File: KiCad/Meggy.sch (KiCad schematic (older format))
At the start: 19 parts, among them J1 USB_B_Micro, J2 Conn_01x03, Q1 DMP2305U-7, Q2 DMP2305U-7, U1 ROM-socket-42pin, U2 AT90USB1286-MU, U3 M29F160F, X1 Standard_Clock_Oscillators_XT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

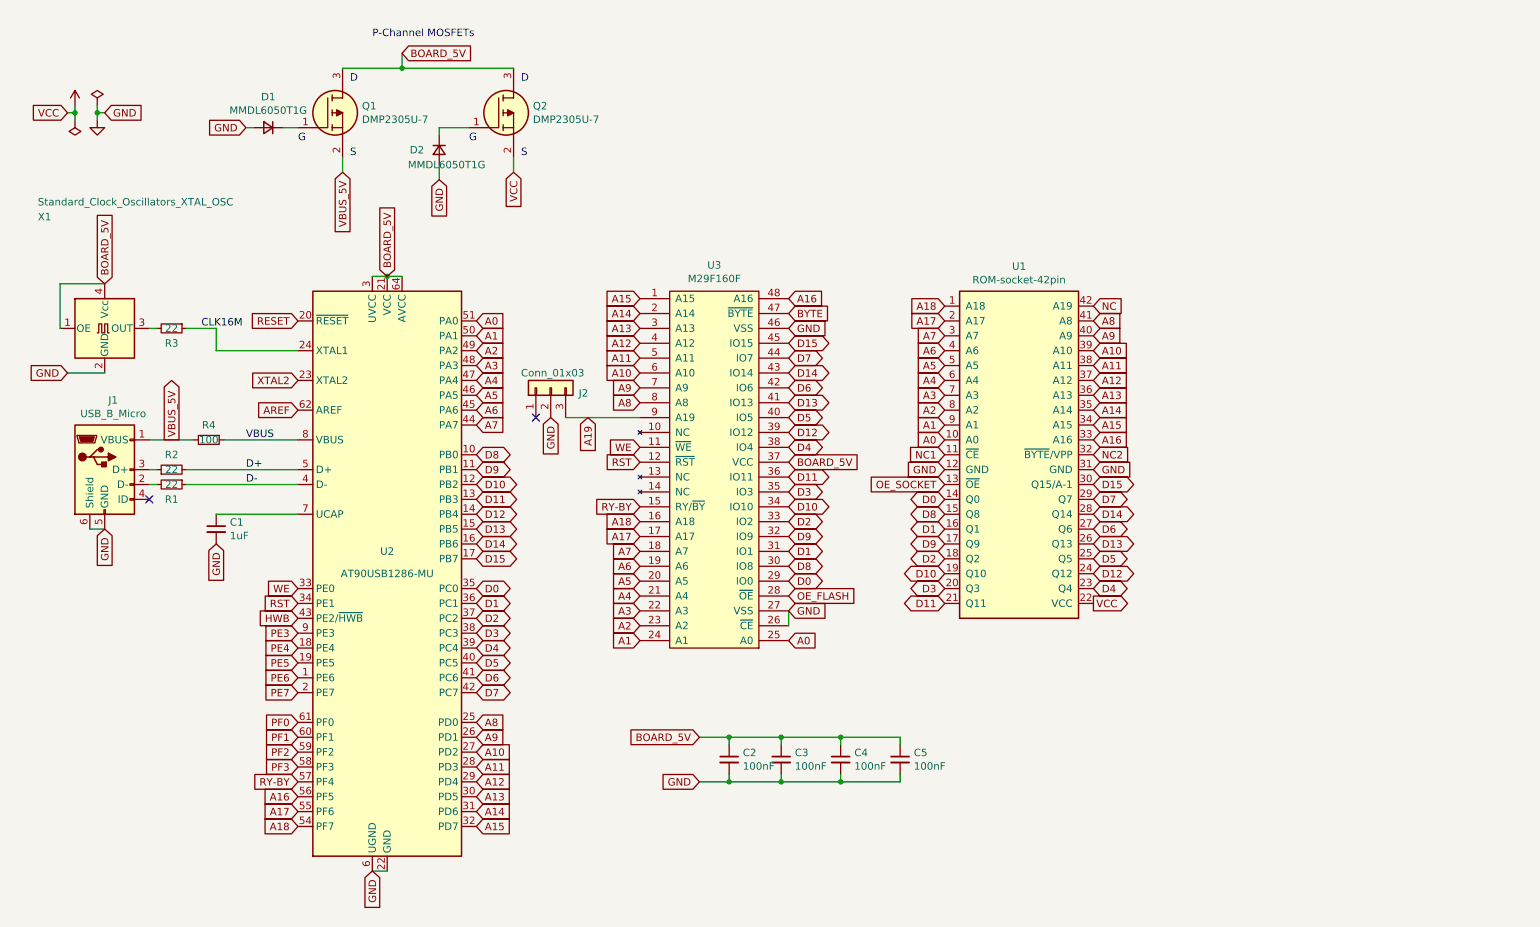
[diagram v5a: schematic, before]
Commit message: Add circuit for controlling Flash-OE signal
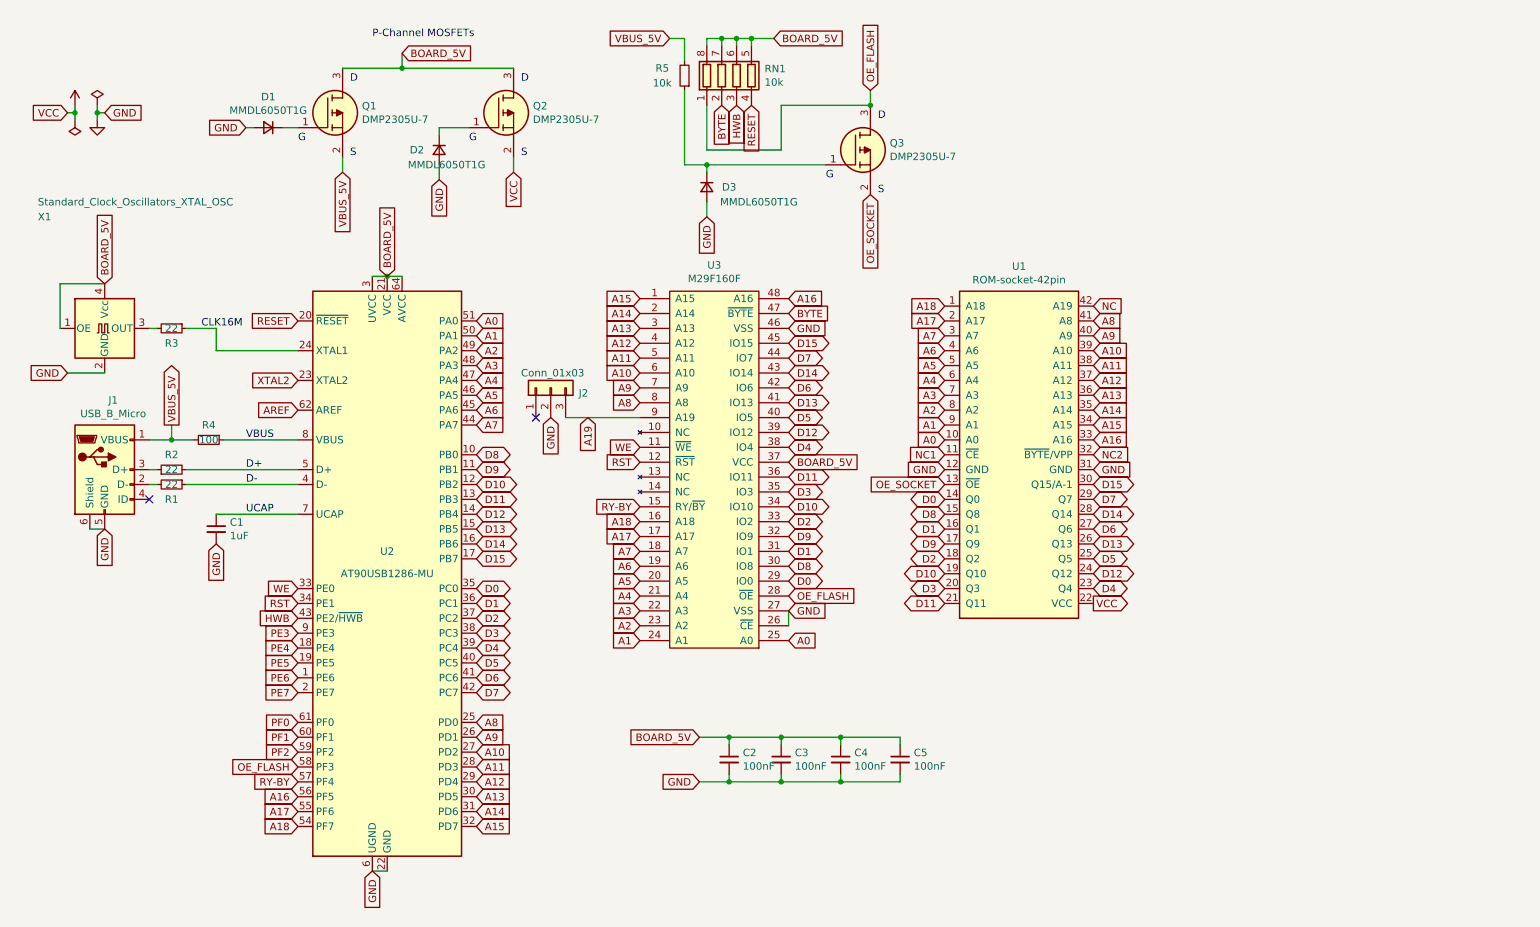
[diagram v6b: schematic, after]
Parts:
- added D3: MMDL6050T1G, Meggy:D_0603_1608Metric_Pad_0.975x0.95mm_HandSolder, symbol Device:D_Small
- added Q3: DMP2305U-7, Package_TO_SOT_SMD:SOT-23, symbol Meggy:DMP2305U-7
- added R5: 10k, Resistor_SMD:R_0603_1608Metric, symbol Device:R_Small
- added RN1: 10k, Meggy:RESCAF80P320X160X60-8N, symbol Device:R_Pack04
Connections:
- net PF3 is gone; now on net OE_FLASH: U2.58 (PF3)
- net BOARD_5V: now also RN1.5 (R4.2), RN1.6 (R3.2), RN1.7 (R2.2), RN1.8 (R1.2)
- net BYTE: now also RN1.2 (R2.1)
- net GND: now also D3.2 (A)
- net HWB: now also RN1.3 (R3.1)
- net OE_FLASH: now also Q3.3, RN1.1 (R1.1)
- net OE_SOCKET: now also Q3.2
- net RESET: now also RN1.4 (R4.1)
- net VBUS_5V: now also R5.2
- net UCAP: now reaches C1.1, U2.7 (UCAP)
- new net: D3.1 (K), Q3.1, R5.1
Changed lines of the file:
@@
 	2550 3350 2050 3350
 Wire Wire Line
-	1550 3350 1850 3350
+	1550 3350 1700 3350
 Text Label 2200 3550 0    50   ~ 0
 D+
@@
 Text GLabel 2550 5450 0    50   Input ~ 0
 PF2
-Text GLabel 2550 5550 0    50   Input ~ 0
-PF3
 Text GLabel 2550 4850 0    50   Input ~ 0
 PE5
@@
 Text GLabel 5850 4400 2    50   Input ~ 0
 OE_FLASH
-Text GLabel 6900 3650 0    50   Input ~ 0
-OE_SOCKET
 Text GLabel 2550 5650 0    50   Input ~ 0
 RY-BY
@@
 	1    0    0    -1
 $EndComp
-Text GLabel 1700 3350 1    50   Output ~ 0
+Text GLabel 1700 3250 1    50   Output ~ 0
 VBUS_5V
 Text GLabel 2850 1550 3    50   Input ~ 0
@@
 Wire Wire Line
 	3500 1500 3500 1600
+$Comp
+L Meggy:DMP2305U-7 Q3
+U 1 1 68E4900A
+P 6100 1500
+F 0 "Q3" H 6530 1646 50  0000 L CNN
+F 1 "DMP2305U-7" H 6530 1555 50  0000 L CNN
+F 2 "Package_TO_SOT_SMD:SOT-23" H 6550 1450 50  0001 L CNN
+F 3 "https://www.diodes.com//assets/Datasheets/DMP2305U.pdf" H 6550 1350 50  0001 L CNN
+	1    6100 1500
+	1    0    0    -1
+$EndComp
+Text GLabel 6400 1000 1    50   Input ~ 0
+OE_FLASH
+Text Notes 6100 1600 0    50   ~ 0
+G
+Text Notes 6450 1200 0    50   ~ 0
+D
+Text Notes 6450 1700 0    50   ~ 0
+S
+$Comp
+L Device:R_Pack04 RN1
+U 1 1 68E54917
+P 5500 900
+F 0 "RN1" H 5688 946 50  0000 L CNN
+F 1 "10k" H 5688 855 50  0000 L CNN
+F 2 "Meggy:RESCAF80P320X160X60-8N" V 5775 900 50  0001 C CNN
+F 3 "~" H 5500 900 50  0001 C CNN
+	1    5500 900
+	1    0    0    -1
+$EndComp
+Wire Wire Line
+	5300 1500 6100 1500
+$Comp
+L Device:D_Small D3
+U 1 1 68E5A0C5
+P 5300 1650
+F 0 "D3" V 5300 1800 50  0000 C CNN
+F 1 "MMDL6050T1G" V 5400 2000 50  0000 C CNN
+F 2 "Meggy:D_0603_1608Metric_Pad_0.975x0.95mm_HandSolder" V 5300 1650 50  0001 C CNN
+F 3 "~" V 5300 1650 50  0001 C CNN
+	1    5300 1650
+	0    1    1    0
+$EndComp
+Wire Wire Line
+	5300 1550 5300 1500
+Text GLabel 5300 1850 3    50   Input ~ 0
+GND
+Wire Wire Line
+	5300 1850 5300 1750
+Text GLabel 5750 650  2    50   Input ~ 0
+BOARD_5V
+Wire Wire Line
+	5400 700  5400 650
+Wire Wire Line
+	5400 650  5500 650
+Wire Wire Line
+	5500 700  5500 650
+Connection ~ 5500 650
+Wire Wire Line
+	5500 650  5600 650
+Wire Wire Line
+	5600 700  5600 650
+Connection ~ 5600 650
+Wire Wire Line
+	5600 650  5750 650
+Wire Wire Line
+	6400 1000 6400 1100
+Text GLabel 5600 1100 3    50   Input ~ 0
+RESET
+Text GLabel 5500 1100 3    50   Input ~ 0
+HWB
+Text GLabel 5050 650  0    50   Input ~ 0
+VBUS_5V
+Wire Wire Line
+	5300 1500 5150 1500
+Connection ~ 5300 1500
+Wire Wire Line
+	5300 1100 5300 1400
+Wire Wire Line
+	5300 1400 5800 1400
+Wire Wire Line
+	5800 1400 5800 1100
+Wire Wire Line
+	5800 1100 6400 1100
+Connection ~ 6400 1100
+Wire Wire Line
+	5400 650  5300 650
+Wire Wire Line
+	5300 650  5300 700
+Connection ~ 5400 650
+Text GLabel 5400 1100 3    50   Input ~ 0
+BYTE
+$Comp
+L Device:R_Small R5
+U 1 1 68EC4E2C
+P 5150 900
+F 0 "R5" H 5300 850 50  0000 C CNN
+F 1 "10k" H 5300 950 50  0000 C CNN
+F 2 "Resistor_SMD:R_0603_1608Metric" H 5150 900 50  0001 C CNN
+F 3 "~" H 5150 900 50  0001 C CNN
+	1    5150 900
+	-1   0    0    1
+$EndComp
+Wire Wire Line
+	5050 650  5150 650
+Wire Wire Line
+	5150 650  5150 800
+Wire Wire Line
+	5150 1000 5150 1500
+Wire Wire Line
+	1700 3250 1700 3350
+Connection ~ 1700 3350
+Wire Wire Line
+	1700 3350 1850 3350
+Text Label 2200 3850 0    50   ~ 0
+UCAP
+Text GLabel 2550 5550 0    50   Input ~ 0
+OE_FLASH
+Text GLabel 6400 1700 3    50   Input ~ 0
+OE_SOCKET
+Text GLabel 6900 3650 0    50   Input ~ 0
+OE_SOCKET
 $EndSCHEMATC

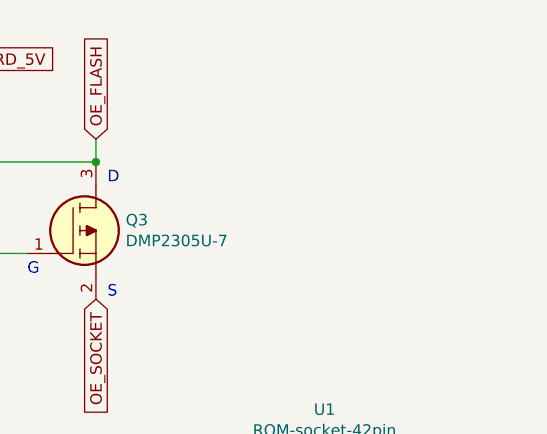
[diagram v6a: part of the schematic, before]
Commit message: Add 10k pull-up resistor network for RY-BY, WE, RST and A19 signals
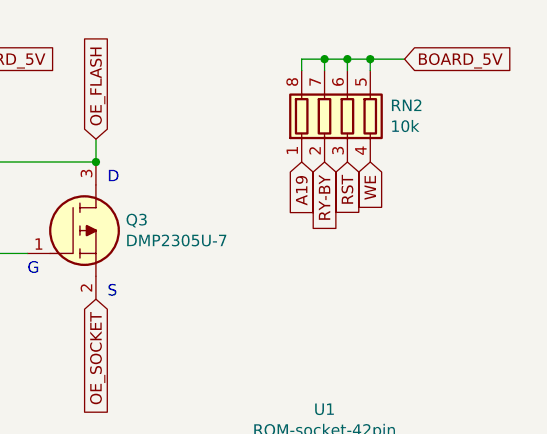
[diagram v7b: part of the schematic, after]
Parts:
- added RN2: 10k, Meggy:RESCAF80P320X160X60-8N, symbol Device:R_Pack04
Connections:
- net A19: now also RN2.1 (R1.1)
- net BOARD_5V: now also RN2.5 (R4.2), RN2.6 (R3.2), RN2.7 (R2.2), RN2.8 (R1.2)
- net RST: now also RN2.3 (R3.1)
- net RY-BY: now also RN2.2 (R2.1)
- net WE: now also RN2.4 (R4.1)
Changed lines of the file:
@@
 Text GLabel 6900 3650 0    50   Input ~ 0
 OE_SOCKET
+$Comp
+L Device:R_Pack04 RN2
+U 1 1 68F0018D
+P 7500 900
+F 0 "RN2" H 7688 946 50  0000 L CNN
+F 1 "10k" H 7688 855 50  0000 L CNN
+F 2 "Meggy:RESCAF80P320X160X60-8N" V 7775 900 50  0001 C CNN
+F 3 "~" H 7500 900 50  0001 C CNN
+	1    7500 900
+	1    0    0    -1
+$EndComp
+Text GLabel 7750 650  2    50   Input ~ 0
+BOARD_5V
+Wire Wire Line
+	7400 700  7400 650
+Wire Wire Line
+	7400 650  7500 650
+Wire Wire Line
+	7500 700  7500 650
+Connection ~ 7500 650
+Wire Wire Line
+	7500 650  7600 650
+Wire Wire Line
+	7600 700  7600 650
+Connection ~ 7600 650
+Wire Wire Line
+	7600 650  7750 650
+Wire Wire Line
+	7400 650  7300 650
+Wire Wire Line
+	7300 650  7300 700
+Connection ~ 7400 650
+Text GLabel 7400 1100 3    50   Input ~ 0
+RY-BY
+Text GLabel 7300 1100 3    50   Input ~ 0
+A19
+Text GLabel 7600 1100 3    50   Input ~ 0
+WE
+Text GLabel 7500 1100 3    50   Input ~ 0
+RST
 $EndSCHEMATC

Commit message: Fix footprint for diode D3 and silkscreen fixes
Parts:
- D3: footprint Meggy:D_0603_1608Metric_Pad_0.975x0.95mm_HandSolder -> Diode_SMD:D_SOD-523
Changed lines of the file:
@@
 F 0 "D3" V 5300 1800 50  0000 C CNN
 F 1 "MMDL6050T1G" V 5400 2000 50  0000 C CNN
-F 2 "Meggy:D_0603_1608Metric_Pad_0.975x0.95mm_HandSolder" V 5300 1650 50  0001 C CNN
+F 2 "Diode_SMD:D_SOD-523" V 5300 1650 50  0001 C CNN
 F 3 "~" V 5300 1650 50  0001 C CNN
 	1    5300 1650
